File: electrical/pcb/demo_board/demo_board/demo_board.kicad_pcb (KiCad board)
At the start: 2 copper layers, 62 x 80.2 mm, 161 parts, among them J0 Conn_01x06_Socket, J1 Conn_01x06_Socket, J10 Conn_01x06_Socket, J11 Conn_01x06_Socket, J2 Conn_01x06_Socket, J3 Conn_01x06_Socket, J4 Conn_01x06_Socket, J5 Conn_01x02_Socket, J6 Conn_01x02_Socket, J7 Conn_01x06_Socket, J8 Conn_01x06_Pin, J9 Conn_01x06_Socket, Q1 NMOS, Q10 NMOS, Q11 NMOS, Q12 NMOS, Q13 PMOS, Q14 PMOS, Q15 PMOS, Q16 PMOS, Q17 PMOS, Q18 PMOS, Q19 NMOS, Q2 PMOS, Q20 NMOS, Q21 NMOS, Q22 PMOS, Q23 PMOS, Q24 PMOS, Q25 NMOS, Q26 NMOS, Q27 NMOS, Q28 PMOS, Q29 PMOS, Q3 NMOS, Q30 PMOS, Q31 NMOS, Q32 NMOS, Q33 NMOS, Q34 PMOS, Q35 PMOS, Q36 PMOS, Q37 NMOS, Q38 NMOS, Q39 NMOS, Q4 NMOS, Q40 PMOS, Q41 PMOS, Q42 PMOS, Q43 NMOS, Q44 NMOS, Q45 NMOS, Q46 PMOS, Q47 PMOS, Q48 PMOS, Q5 PMOS, Q6 NMOS, Q7 PMOS, Q8 NMOS, Q9 NMOS, U1 74HC595, U2 74HC595, U3 74HC595, U4 SN74LV4T125

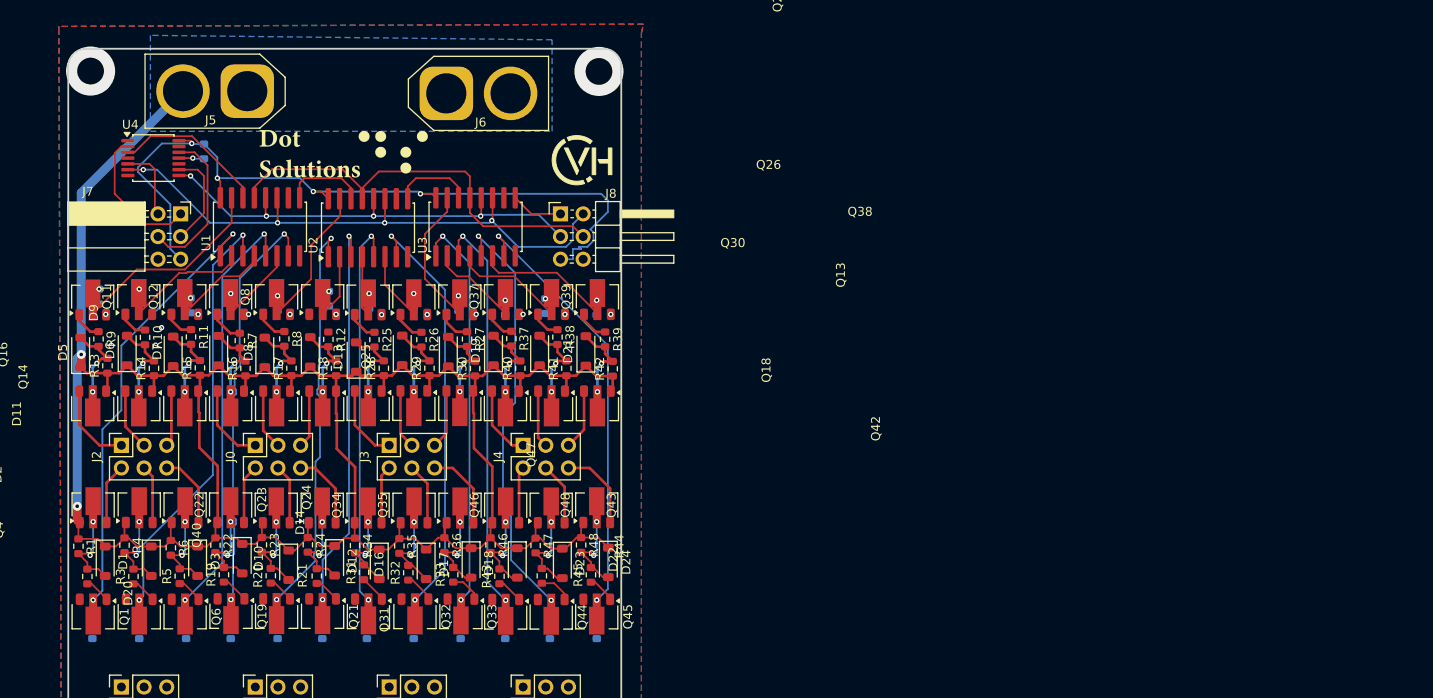
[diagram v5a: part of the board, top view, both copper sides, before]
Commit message: ordered boards
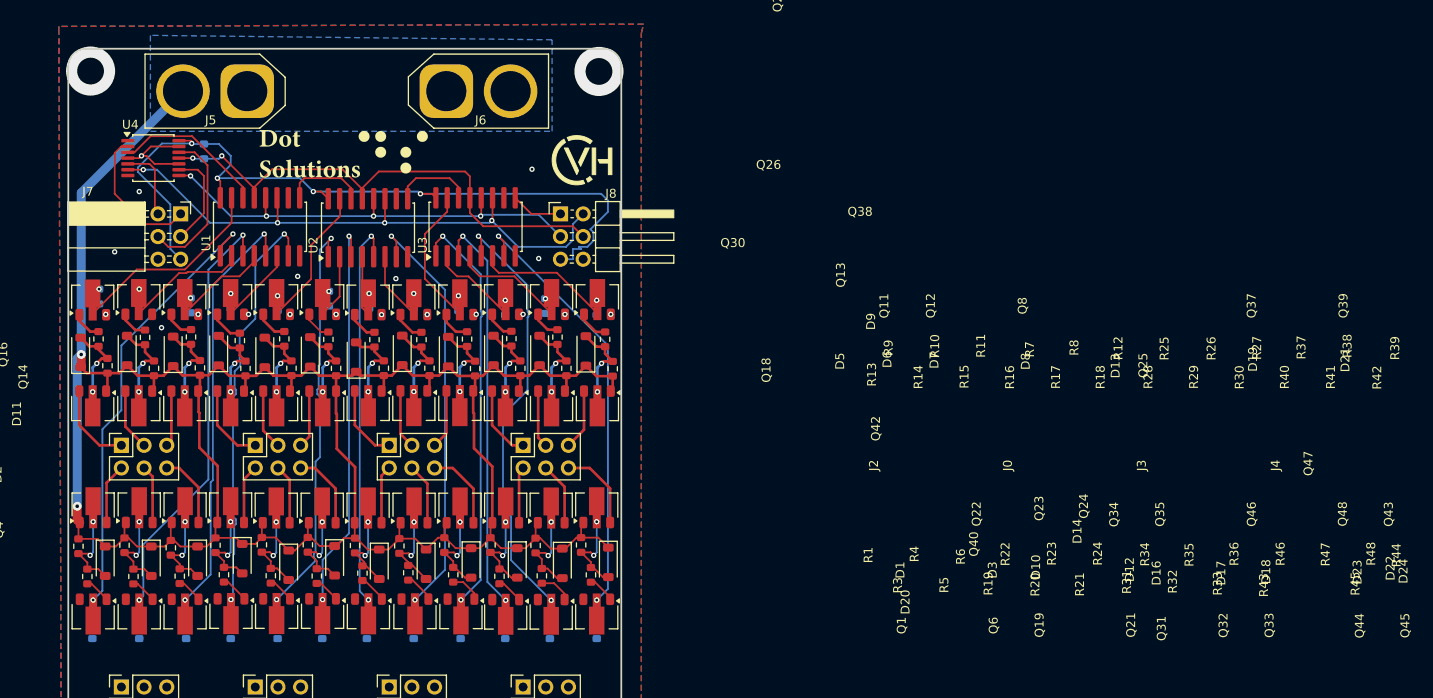
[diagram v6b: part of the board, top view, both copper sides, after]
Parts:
- moved J6 0.25 mm to (81.4, 66.2)
- moved R31 0.20 mm to (72.0, 120.2)
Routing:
- net GND: track 0.00 -> 10.8 mm, vias 16 -> 23
- net OE: track 51.1 -> 59.5 mm, vias 1 -> 2
- net Net-(Q9-D): track 0.00 -> 3.34 mm
- net /DotDriver/UP2: track 50.5 -> 53.2 mm
- net /DotDriver/UP4: track 48.0 -> 50.7 mm
- net +5V: track 89.3 -> 91.5 mm
- net /DotDriver3/UP4: track 50.3 -> 51.6 mm
- net /DotDriver2/UP6: track 47.6 -> 48.7 mm
